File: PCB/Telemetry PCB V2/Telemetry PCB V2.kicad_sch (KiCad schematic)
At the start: 44 parts, among them IC1 E22-900M22S, J1 USB_C_Receptacle_USB2.0_16P, J2 Conn_01x04_Pin, J3 Serial Debug Header 1x4, J4 GPS, J5 Batt, SW1 SW_MEC_5E, SW2 SW_MEC_5E, U1 STM32F411CEUx, U2 MCP1700x-250xxTT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

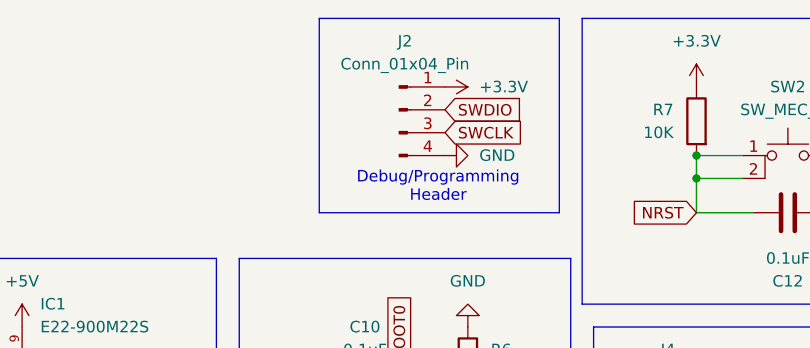
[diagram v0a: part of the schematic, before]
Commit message: Large Board Update
Changed stack-up order to signal-ground-power-signal2

tweaked constraints for vias and spacing then adjusted components to fit

changed stm decoupling capacitors to smaller better placed footprints.
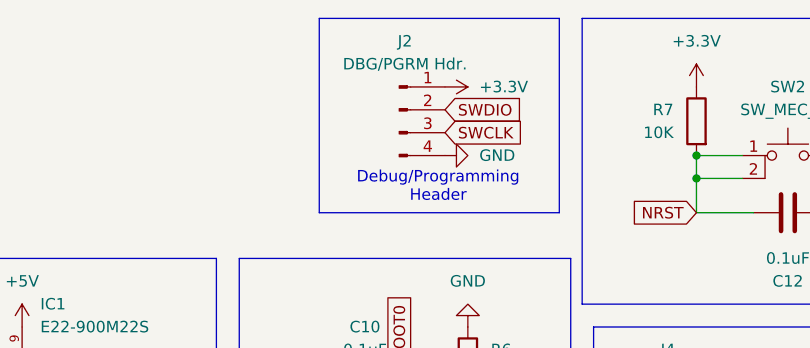
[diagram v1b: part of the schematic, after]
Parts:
- C6, C7, C8, C9: footprint Capacitor_SMD:C_1206_3216Metric_Pad1.33x1.80mm_HandSolder -> Capacitor_SMD:C_0603_1608Metric_Pad1.08x0.95mm_HandSolder
- J2: value Conn_01x04_Pin -> DBG/PGRM Hdr.
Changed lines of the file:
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@@
 			)
 		)
-		(property "Footprint" "Capacitor_SMD:C_1206_3216Metric_Pad1.33x1.80mm_HandSolder"
+		(property "Footprint" "Capacitor_SMD:C_0603_1608Metric_Pad1.08x0.95mm_HandSolder"
 			(at 82.8548 35.56 0)
 			(effects
@@
 			)
 		)
-		(property "Footprint" "Capacitor_SMD:C_1206_3216Metric_Pad1.33x1.80mm_HandSolder"
+		(property "Footprint" "Capacitor_SMD:C_0603_1608Metric_Pad1.08x0.95mm_HandSolder"
 			(at 74.93 21.8948 0)
 			(effects
@@
 			)
 		)
-		(property "Footprint" "Capacitor_SMD:C_1206_3216Metric_Pad1.33x1.80mm_HandSolder"
+		(property "Footprint" "Capacitor_SMD:C_0603_1608Metric_Pad1.08x0.95mm_HandSolder"
 			(at 64.77 30.7848 0)
 			(effects
@@
 			)
 		)
-		(property "Footprint" "Capacitor_SMD:C_1206_3216Metric_Pad1.33x1.80mm_HandSolder"
+		(property "Footprint" "Capacitor_SMD:C_0603_1608Metric_Pad1.08x0.95mm_HandSolder"
 			(at 77.47 30.7848 0)
 			(effects
@@
 			)
 		)
-		(property "Value" "Conn_01x04_Pin"
+		(property "Value" "DBG/PGRM Hdr."
 			(at 169.545 20.32 0)
 			(effects

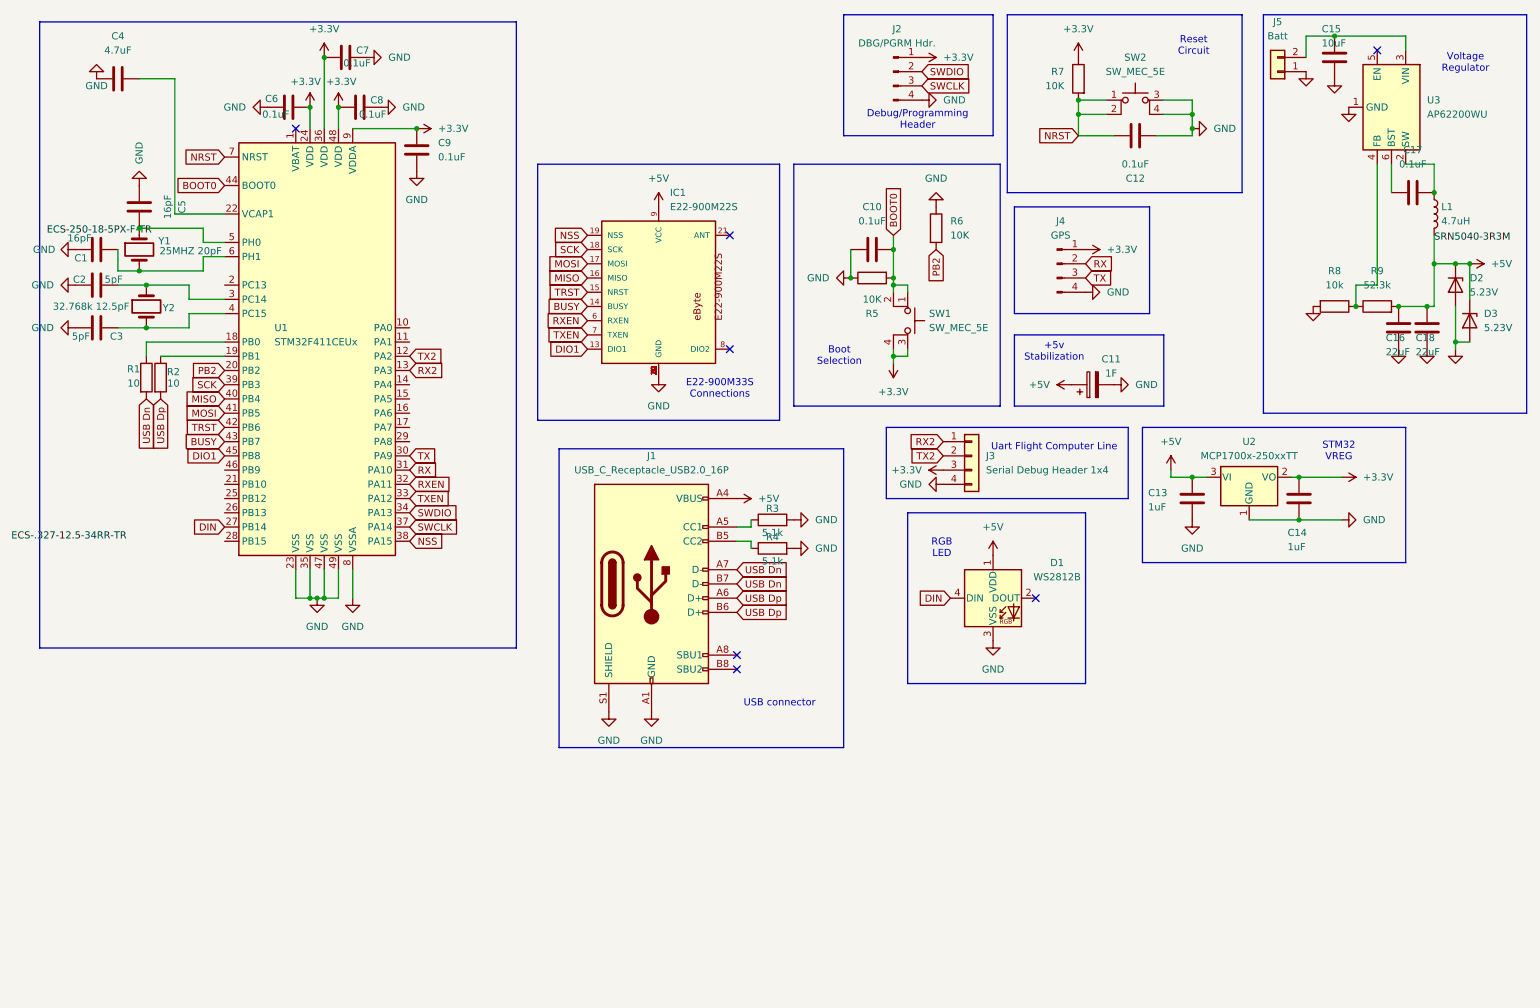
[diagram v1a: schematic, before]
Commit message: Broad tweaks
Tweaked the location of many power components by small amounts.

Changed to two 1000uF capacitors foe smoothing

swapped Flight computer pin header to 3 pin jst-xh
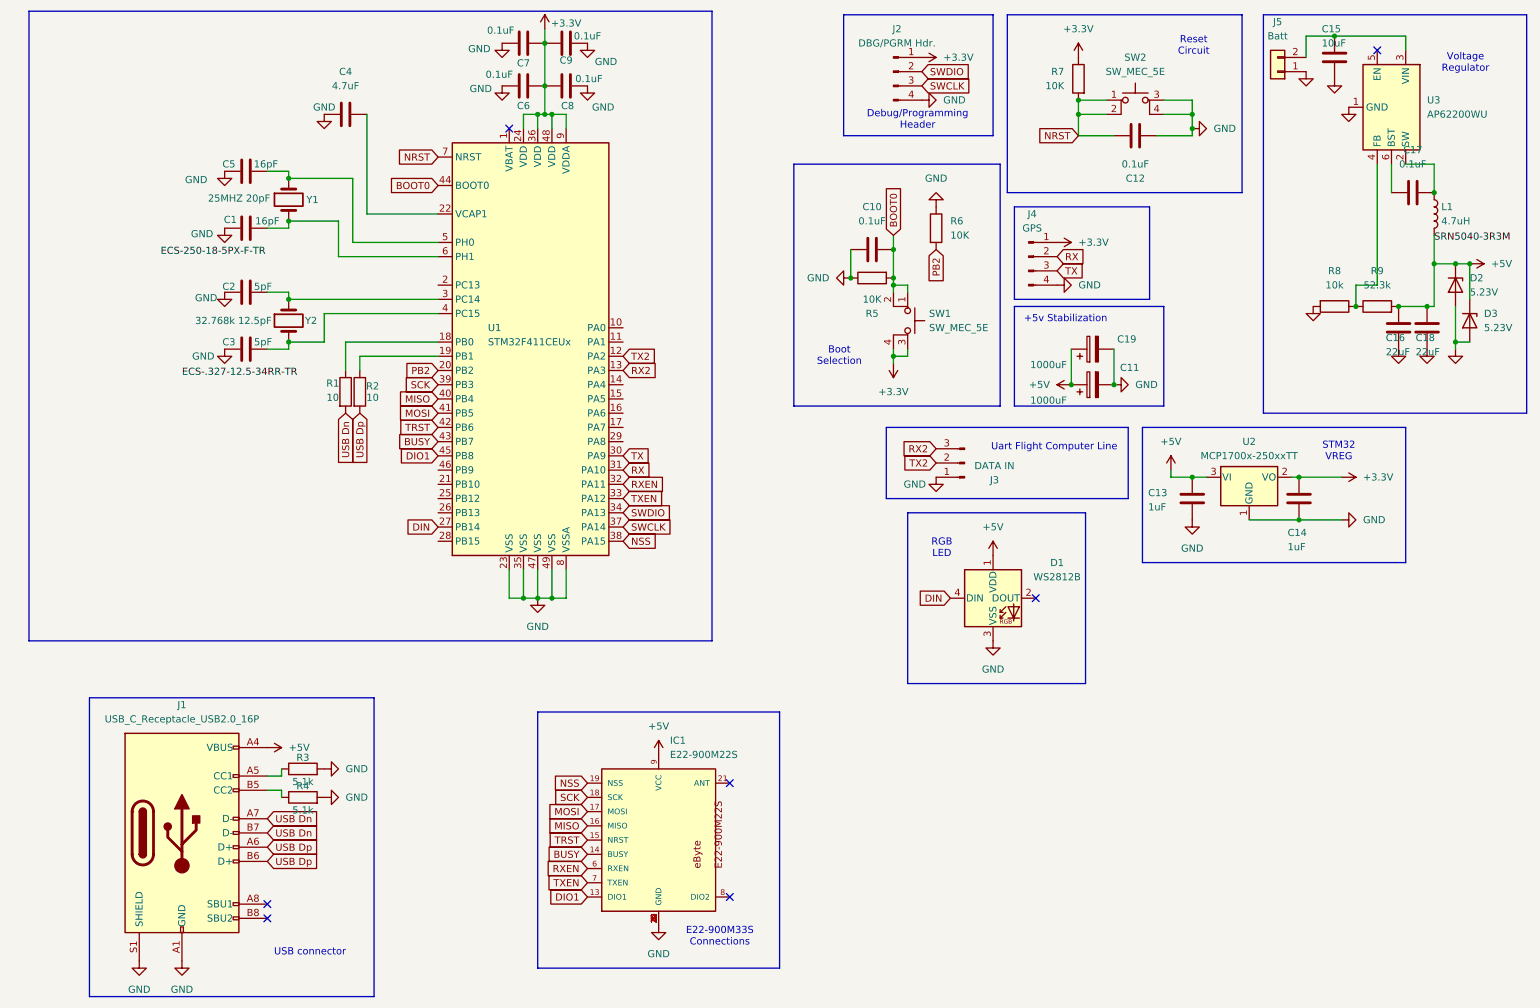
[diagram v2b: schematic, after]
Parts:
- removed J3: Serial Debug Header 1x4, Connector_PinHeader_2.54mm:PinHeader_1x04_P2.54mm_Vertical, symbol Connector_Generic:Conn_01x04
- added C19: 1000uF, Capacitor_THT:CP_Radial_D12.5mm_P5.00mm, symbol Device:C_Polarized
- added J3: DATA IN, Connector_JST:JST_XH_B3B-XH-A_1x03_P2.50mm_Vertical, symbol Connector:Conn_01x03_Pin
- C11: value 1F -> 1000uF; footprint Custom Capacitor:C_Rect_L16.5mm_W8.7mm_P12.00mm_MKT -> Capacitor_THT:CP_Radial_D12.5mm_P5.00mm
- J1: footprint Connector_USB:USB_C_Receptacle_GCT_USB4105-xx-A_16P_TopMnt_Horizontal -> Custom Capacitor:USB_C_Receptacle_HCTL_HC-TYPE-C-16P-01A (SMALLER PADS)
- J5: footprint Connector_JST:JST_XH_B2B-XH-AM_1x02_P2.50mm_Vertical -> Connector_JST:JST_XH_B2B-XH-A_1x02_P2.50mm_Vertical
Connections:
- net +5V: now also C19.1
- net GND: now also C19.2, J3.1 (Pin_1)
- net RX2: now also J3.3 (Pin_3)
- net TX2: now also J3.2 (Pin_2)
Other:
- moved on the sheet: C1, C2, C3, C4, C5, C6, C7, C8, C9, IC1, J1, J4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

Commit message: added test points
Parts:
- added TP1, TP2, TP3, TP4, TP5: TestPoint, TestPoint:TestPoint_Loop_D1.80mm_Drill1.0mm_Beaded, symbol Connector:TestPoint
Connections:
- net +3.3V: now also TP3.1
- net +5V: now also TP1.1, TP2.1
- net GND: now also TP4.1, TP5.1
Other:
- moved on the sheet: D3

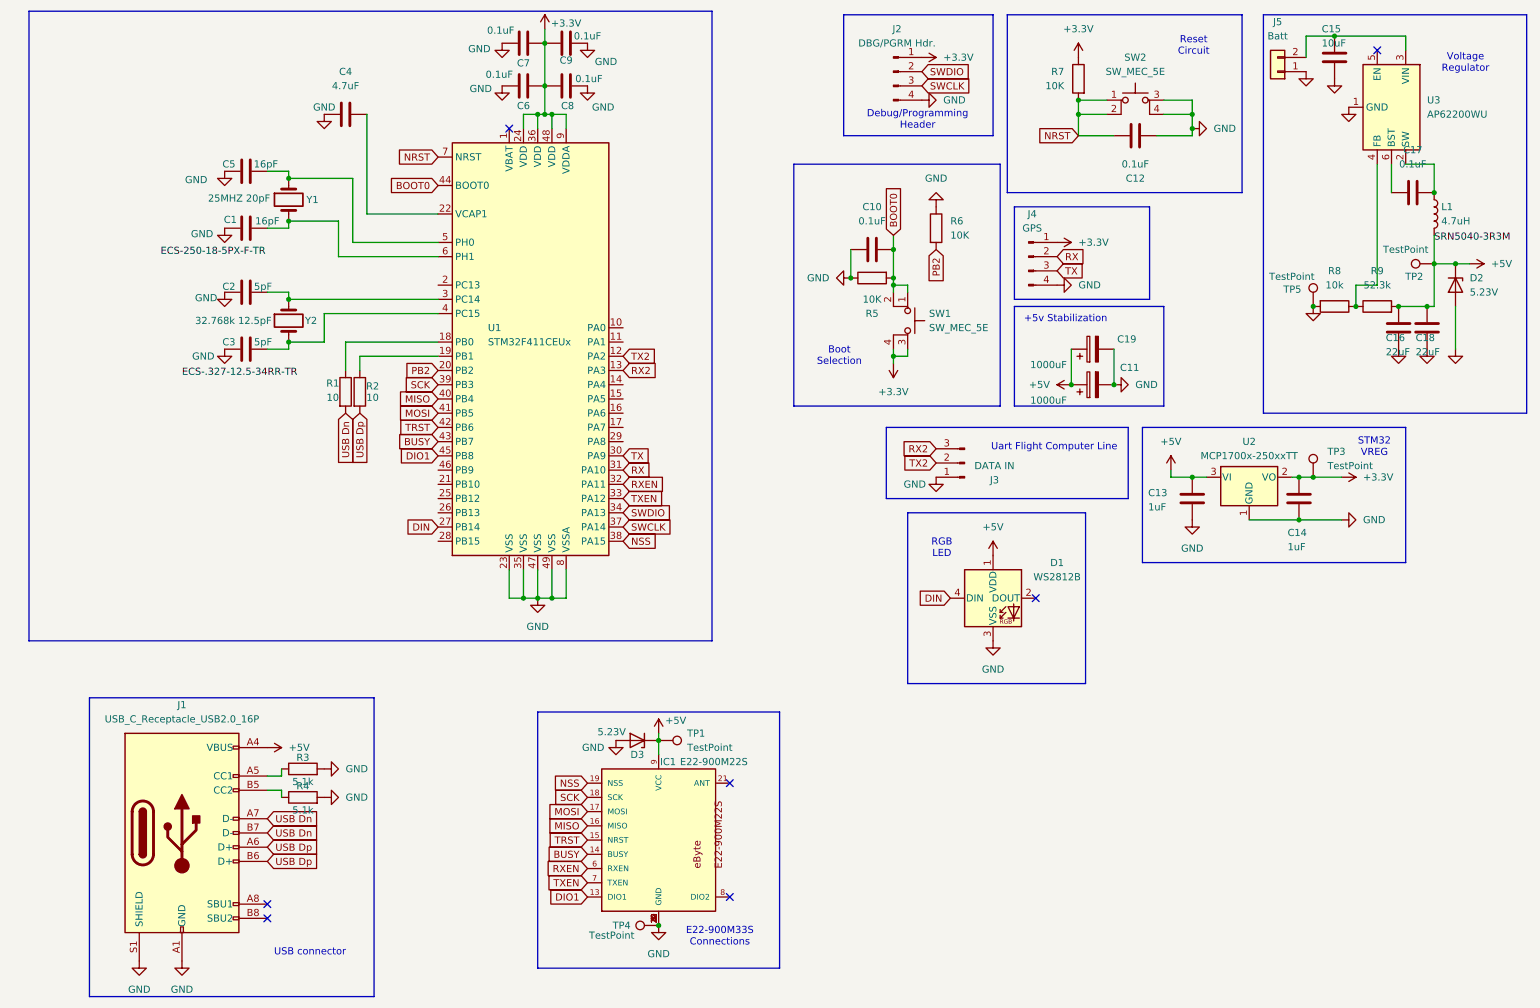
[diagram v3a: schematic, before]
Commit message: :D
board is done as best I can tell

This update fully removed the smoothing caps as experienced people don't believe they are necessary. This resulted in moving a couple components around.

The vias greater than 0.5mm have had solder mask free zones added on them to prevent JLC from trying plug them because JLC says that plugging is likely to fail on large vias.
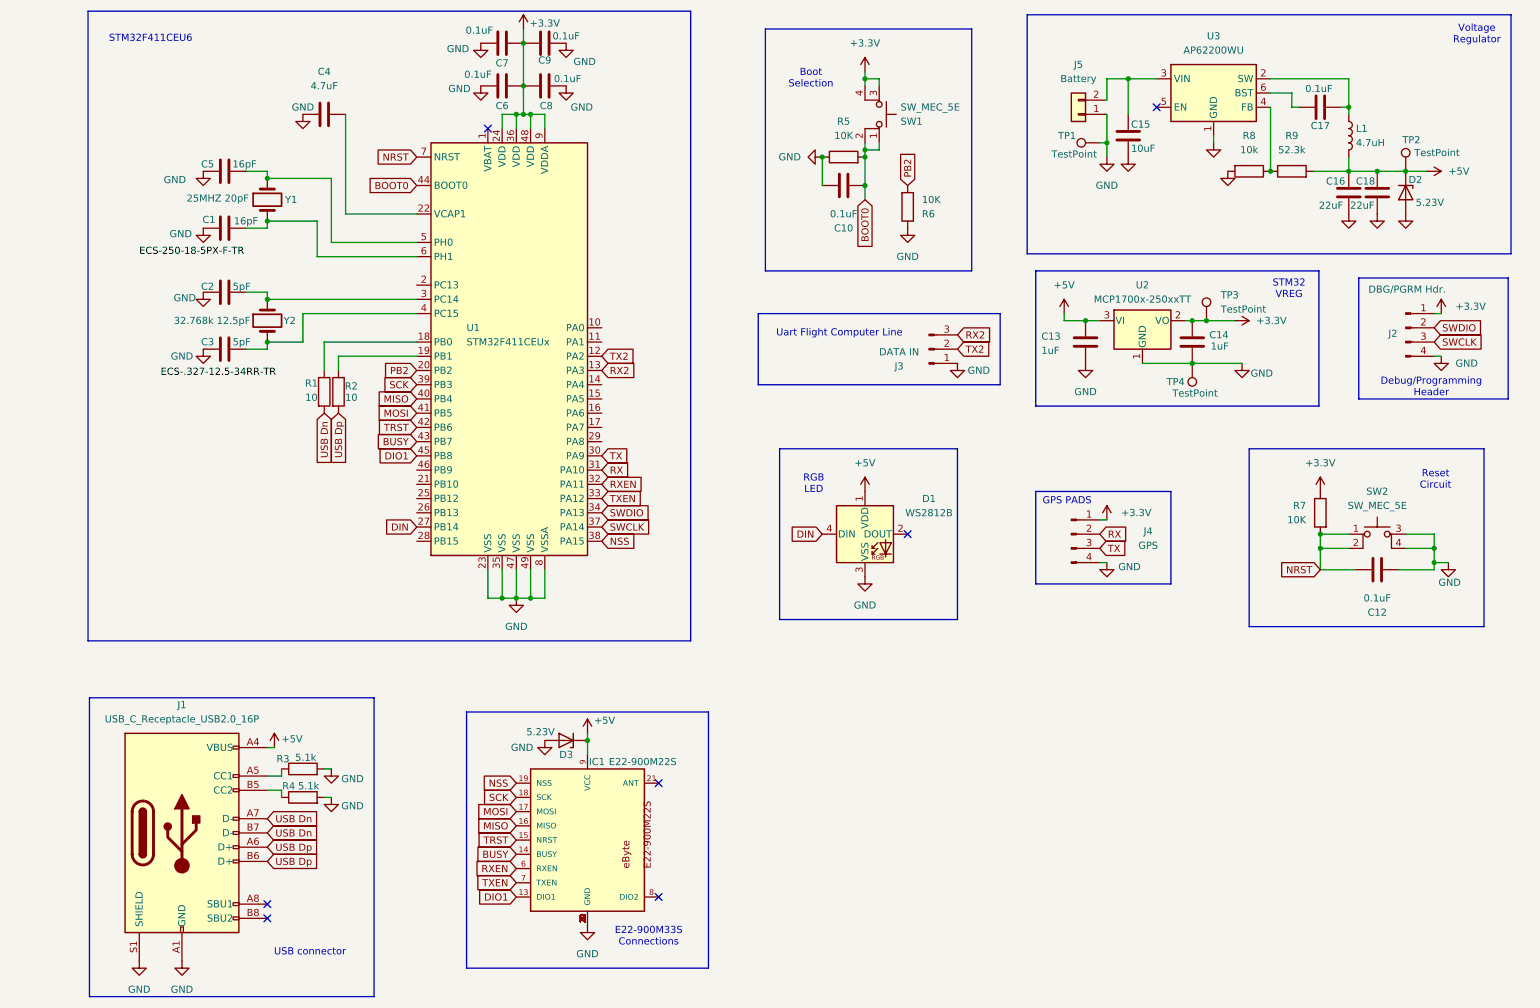
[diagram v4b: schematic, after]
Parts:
- removed C11, C19: 1000uF, Capacitor_THT:CP_Radial_D12.5mm_P5.00mm, symbol Device:C_Polarized
- removed TP1, TP5: TestPoint, TestPoint:TestPoint_Loop_D1.80mm_Drill1.0mm_Beaded, symbol Connector:TestPoint
- added TP4: TestPoint, TestPoint:TestPoint_Loop_D1.80mm_Drill1.0mm_Beaded, symbol Connector:TestPoint
- J5: value Batt -> Battery
- renumbered TP4 to TP1
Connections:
- net GND: now also TP4.1
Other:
- note added: "GPS PADS"
- note added: "STM32F411CEU6"
- note removed: "+5v Stabilization"
- moved on the sheet: C1, C10, C12, C13, C14, C15, C16, C17, C18, C2, C3, C4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
